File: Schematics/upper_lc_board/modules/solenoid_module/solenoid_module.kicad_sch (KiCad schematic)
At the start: 8 parts

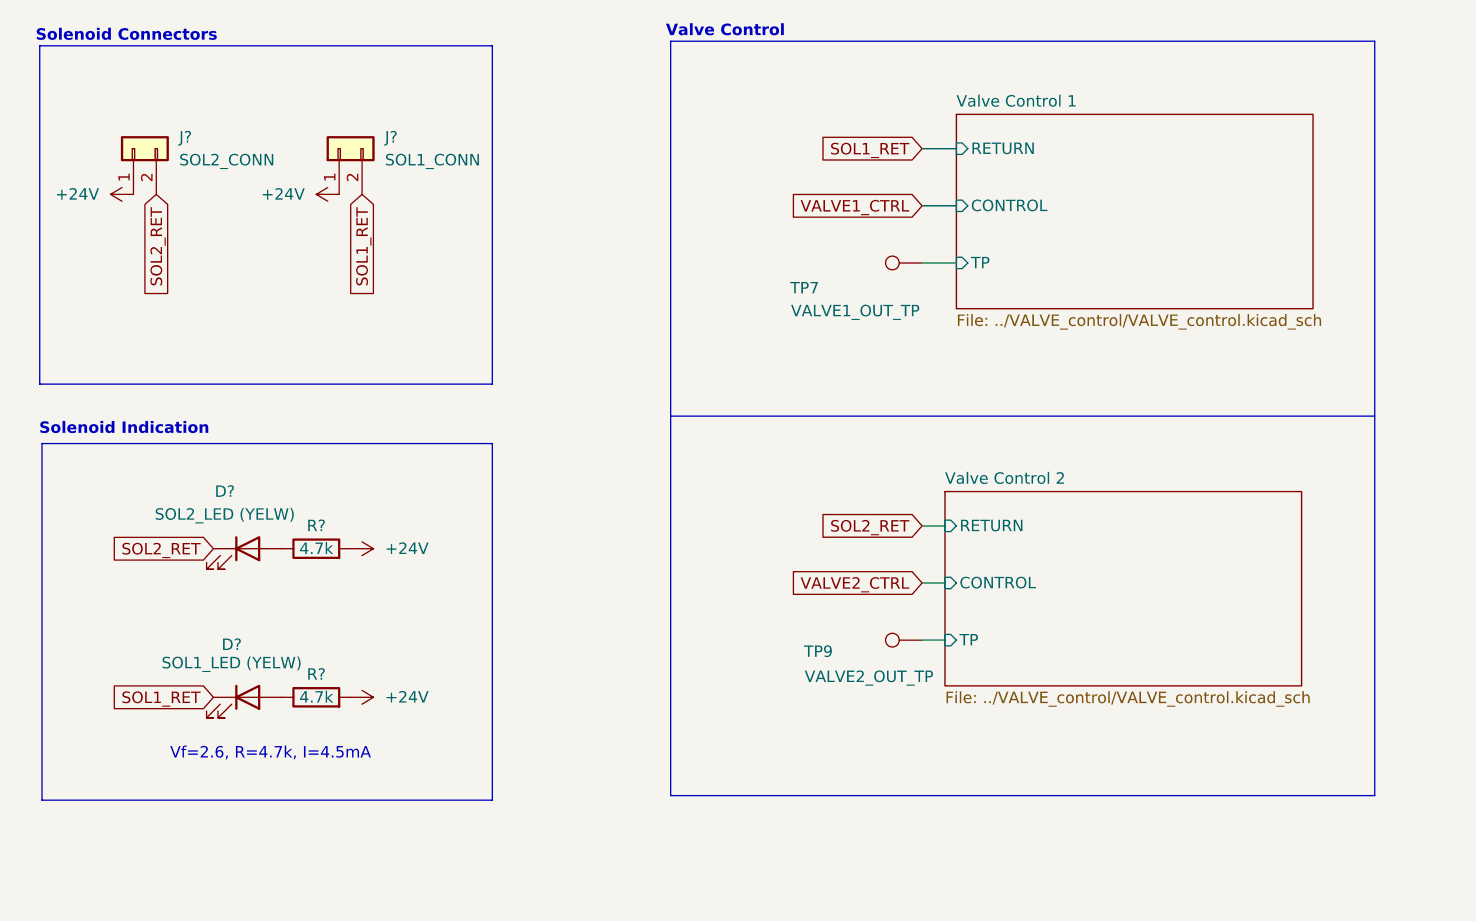
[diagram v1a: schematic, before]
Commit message: add references to caps, ferrite bead footprint, LDO datasheet
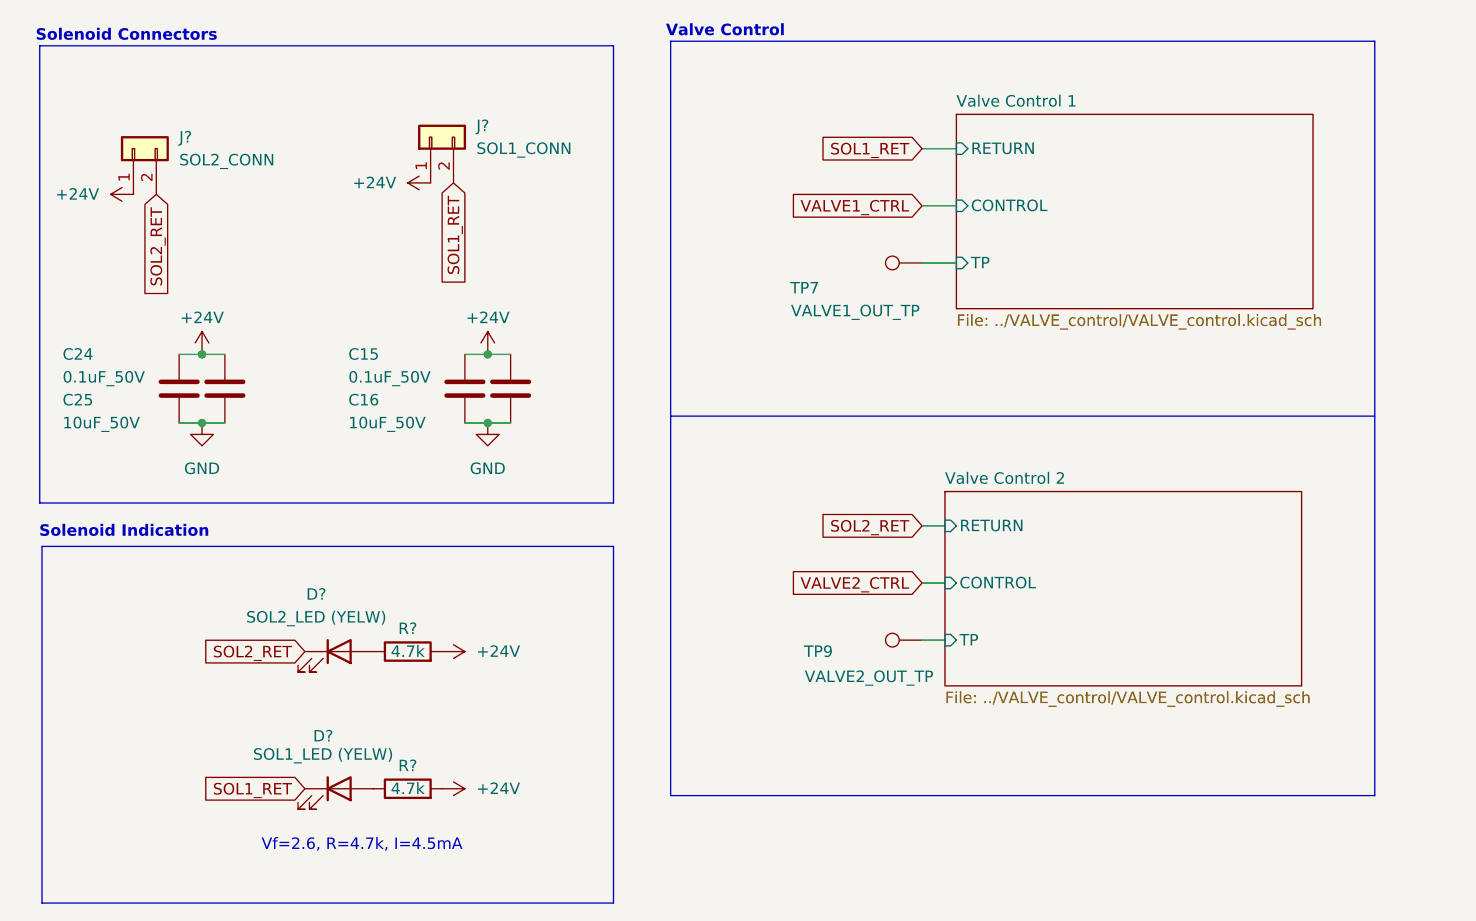
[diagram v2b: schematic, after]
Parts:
- added C15: 0.1uF_50V, Capacitor_SMD:C_0805_2012Metric, symbol Device:C
- added C16: 10uF_50V, Capacitor_SMD:CP_Elec_6.3x5.3, symbol Device:C
- added C24: 0.1uF_50V, Capacitor_SMD:C_0603_1608Metric, symbol Device:C
- added C25: 10uF_50V, Capacitor_SMD:C_1206_3216Metric, symbol Device:C
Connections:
- net +24V: now also C15.1, C16.1, C24.1, C25.1
- new net GND: C15.2, C16.2, C24.2, C25.2
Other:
- moved on the sheet: D?, J?, R?
